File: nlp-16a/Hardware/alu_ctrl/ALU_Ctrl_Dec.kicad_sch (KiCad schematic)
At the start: 9 parts, among them U19 CD74HC00, U20 CD74HC00, U21 CD74HC00, U22 CD74HC00, U23 CD74HC00, U24 CD74HC00, U25 CD74HC00, U26 CD74HC00, U27 CD74HC00

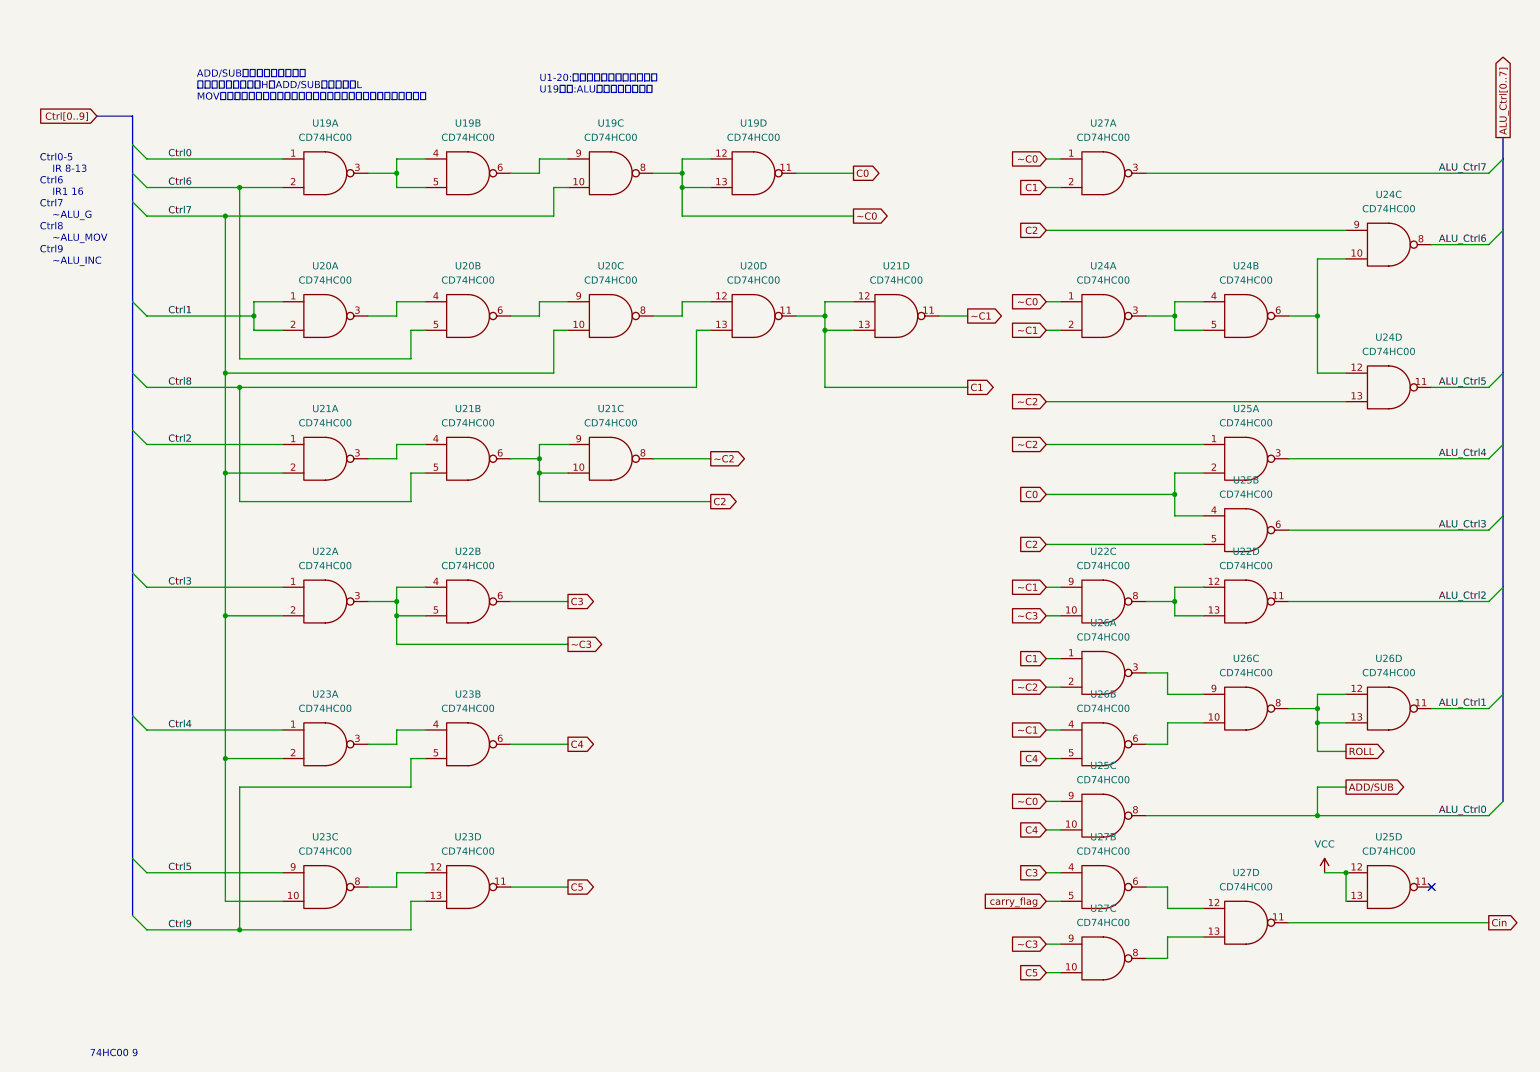
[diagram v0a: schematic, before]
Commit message: ALU制御の回路修正
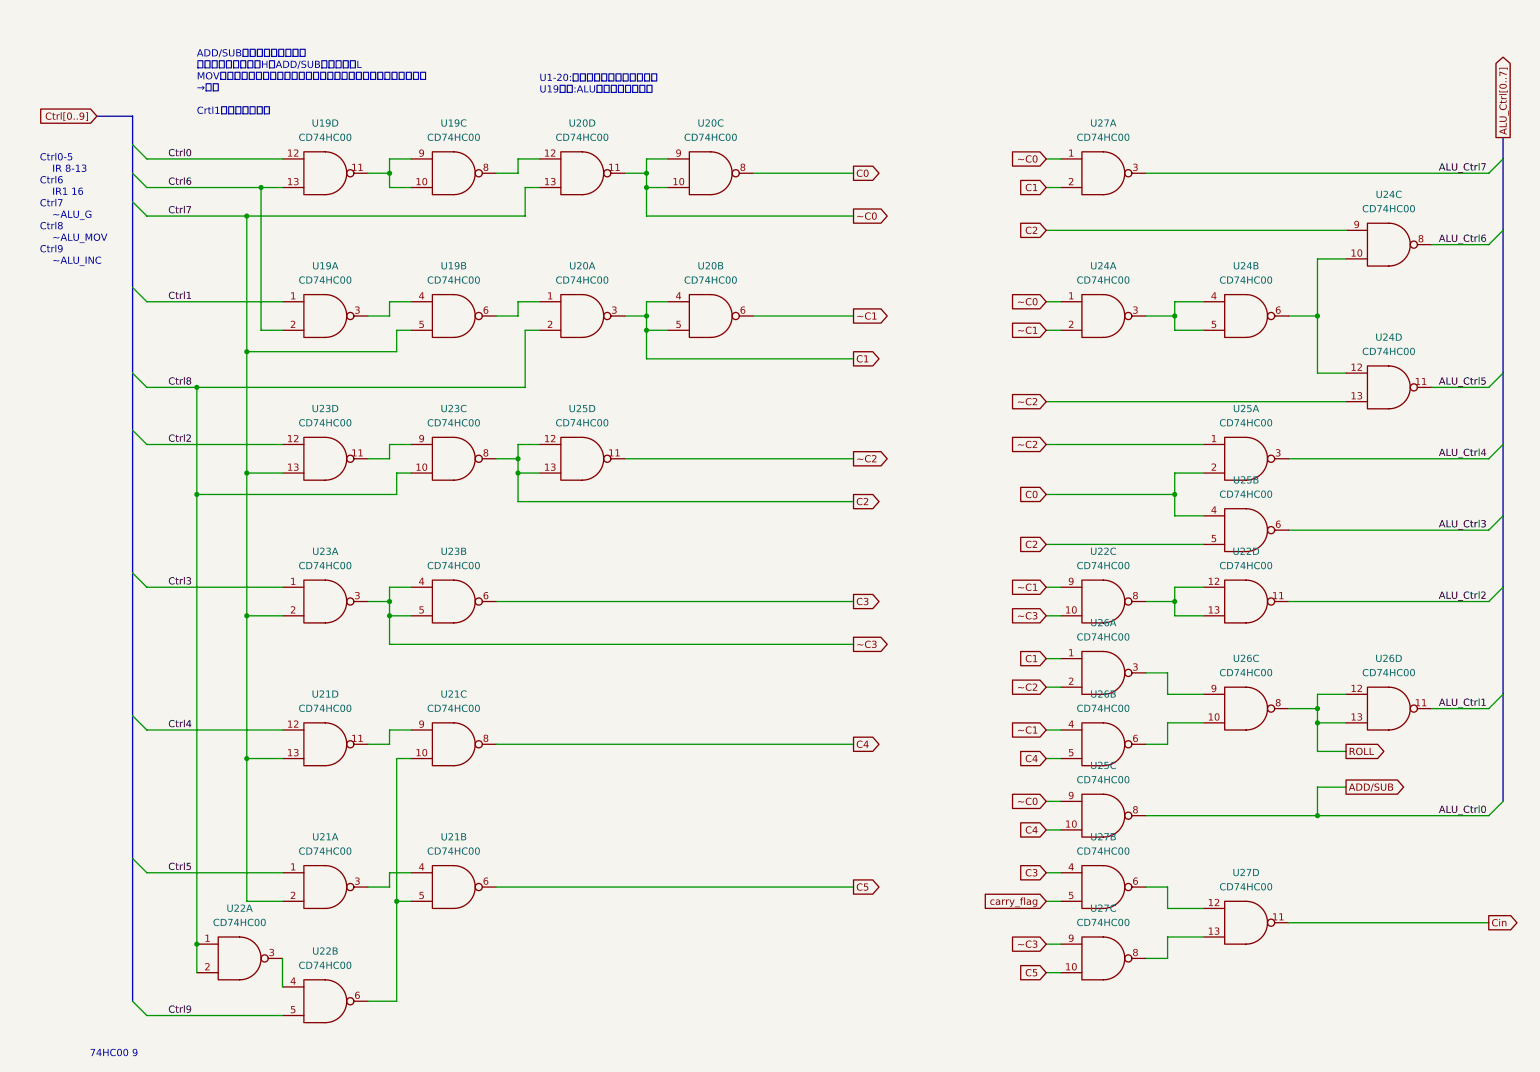
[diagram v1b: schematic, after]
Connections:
- net C0: now also U20.8; no longer U19.11
- net C1: now also U20.3, U20.4, U20.5; no longer U20.11, U21.12, U21.13
- net C2: now also U23.8, U25.12, U25.13; no longer U21.10, U21.6, U21.9
- net C3: now also U23.6; no longer U22.6
- net C4: now also U21.8; no longer U23.6
- net C5: now also U21.6; no longer U23.11
- net Ctrl0: now also U19.12; no longer U19.1
- net Ctrl1: now also U19.1; no longer U20.1, U20.2
- net Ctrl2: now also U23.12; no longer U21.1
- net Ctrl3: now also U23.1; no longer U22.1
- net Ctrl4: now also U21.12; no longer U23.1
- net Ctrl5: now also U21.1; no longer U23.9
- net Ctrl6: now also U19.13; no longer U20.5
- net Ctrl7: now also U19.5, U20.13, U21.13, U23.13; no longer U19.10, U20.10, U22.2, U23.10
- net Ctrl8: now also U20.2, U22.1, U22.2, U23.10; no longer U20.13, U21.5
- net Ctrl9: now also U22.5; no longer U23.13, U23.5
- net VCC: no longer U25.12, U25.13
- net ~C0: now also U20.10, U20.11, U20.9; no longer U19.12, U19.13, U19.8
- net ~C1: now also U20.6; no longer U21.11
- net ~C2: now also U25.11; no longer U21.8
- net ~C3: now also U23.3, U23.4, U23.5; no longer U22.3, U22.4, U22.5
- net at U19.3, U19.4: no longer U19.5
- net at U19.6: now also U20.1; no longer U19.9
- net at U20.12: now also U19.8; no longer U20.8
- new net: U19.10, U19.11, U19.9
- new net: U22.3, U22.4
- new net: U21.10, U21.5, U22.6
- new net: U21.11, U21.9
- new net: U23.11, U23.9
- no-connect marks 1 -> 0
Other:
- note added: "ADD/SUB介入モードに不具合 モード設定が逆通常HでADD/SUBモードのみL MOVモード，通常演算モードに影響を与えない設計にする必要があり →解消 Crtl1デコード不完全"
- note removed: "ADD/SUB介入モードに不具合 モード設定が逆通常HでADD/SUBモードのみL MOVモード，通常演算モードに影響を与えない設計にする必要があり"
- moved on the sheet: U19A, U19B, U19C, U19D, U20A, U20B, U20C, U20D, U21A, U21B, U21C, U21D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

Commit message: ゼロフラグ高速化
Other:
- note added: "ADD/SUB介入モードに不具合 モード設定が逆通常HでADD/SUBモードのみL MOVモード，通常演算モードに影響を与えない設計にする必要があり →解消 Crtl1デコード不完全→解消 最終版→Ctrl1は反転とする．"
- note added: "Ctrl0-5 IR 8-13 Ctrl6 ADDRESS_MODE(IR1 15) Ctrl7 ~INTERNAL_MOV Ctrl8 ~INTERNAL_INC Ctrl9 ~INTERNAL_DEC ADDRESS_MODE: アドレッシング時の演算モードに切り替え．演算命令以外でこのモードになる． INTERNAL_MOV: 内部処理での値を移動するときのモード． ADDRESS_MODEより優先される． INTERNAI_INC: 内部処理でインクリメントするときのモード． このモードを使用する際にはINTERNAL_MOVが有効である必要がある． ADDRESS_MODEより優先される． INTERNAI_INC: 内部処理でデクリメントするときのモード． このモードを使用する際にはINTERNAL_MOV，INTERNAL_INCが有効である必要がある． ADDRESS_M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"
- note removed: "ADD/SUB介入モードに不具合 モード設定が逆通常HでADD/SUBモードのみL MOVモード，通常演算モードに影響を与えない設計にする必要があり →解消 Crtl1デコード不完全"
- note removed: "Ctrl0-5 IR 8-13 Ctrl6 IR1 16 Ctrl7 ~ALU_G Ctrl8 ~ALU_MOV Ctrl9 ~ALU_INC"
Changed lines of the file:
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@@
     (effects (font (size 1.27 1.27)) (justify left bottom))
   )
-  (text "ADD/SUB介入モードに不具合\nモード設定が逆通常HでADD/SUBモードのみL\nMOVモード，通常演算モードに影響を与えない設計にする必要があり\n→解消\n\nCrtl1デコード不完全"
+  (text "ADD/SUB介入モードに不具合\nモード設定が逆通常HでADD/SUBモードのみL\nMOVモード，通常演算モードに影響を与えない設計にする必要があり\n→解消\n\nCrtl1デコード不完全→解消\n\n最終版→Ctrl1は反転とする．"
     (at 41.91 25.4 0)
     (effects (font (size 1.27 1.27)) (justify left bottom))
   )
-  (text "Ctrl0-5\n	IR 8-13\nCtrl6\n	IR1 16\nCtrl7\n	~ALU_G\nCtrl8\n	~ALU_MOV\nCtrl9\n	~ALU_INC"
-    (at 13.97 52.07 0)
+  (text "Ctrl0-5\n	IR 8-13\nCtrl6\n	ADDRESS_MODE(IR1 15)\nCtrl7\n	~INTERNAL_MOV\nCtrl8\n	~INTERNAL_INC\nCtrl9\n	~INTERNAL_DEC\n\nADDRESS_MODE:\n	アドレッシング時の演算モードに切り替え．演算命令以外でこのモードになる．\nINTERNAL_MOV:\n	内部処理での値を移動するときのモード．\n	ADDRESS_MODEより優先される．\nINTERNAI_INC:\n	内部処理でインクリメントするときのモード．\n	このモードを使用する際にはINTERNAL_MOVが有効である必要がある．\n	ADDRESS_MODEより優先される．\nINTERNAI_INC:\n	内部処理でデクリメントするときのモード．\n	このモードを使用する際にはINTERNAL_MOV，INTERNAL_INCが有効である必要がある．\n	ADDRESS_MODEより優先される．"
+    (at 102.87 189.23 0)
     (effects (font (size 1.27 1.27)) (justify left bottom))
   )

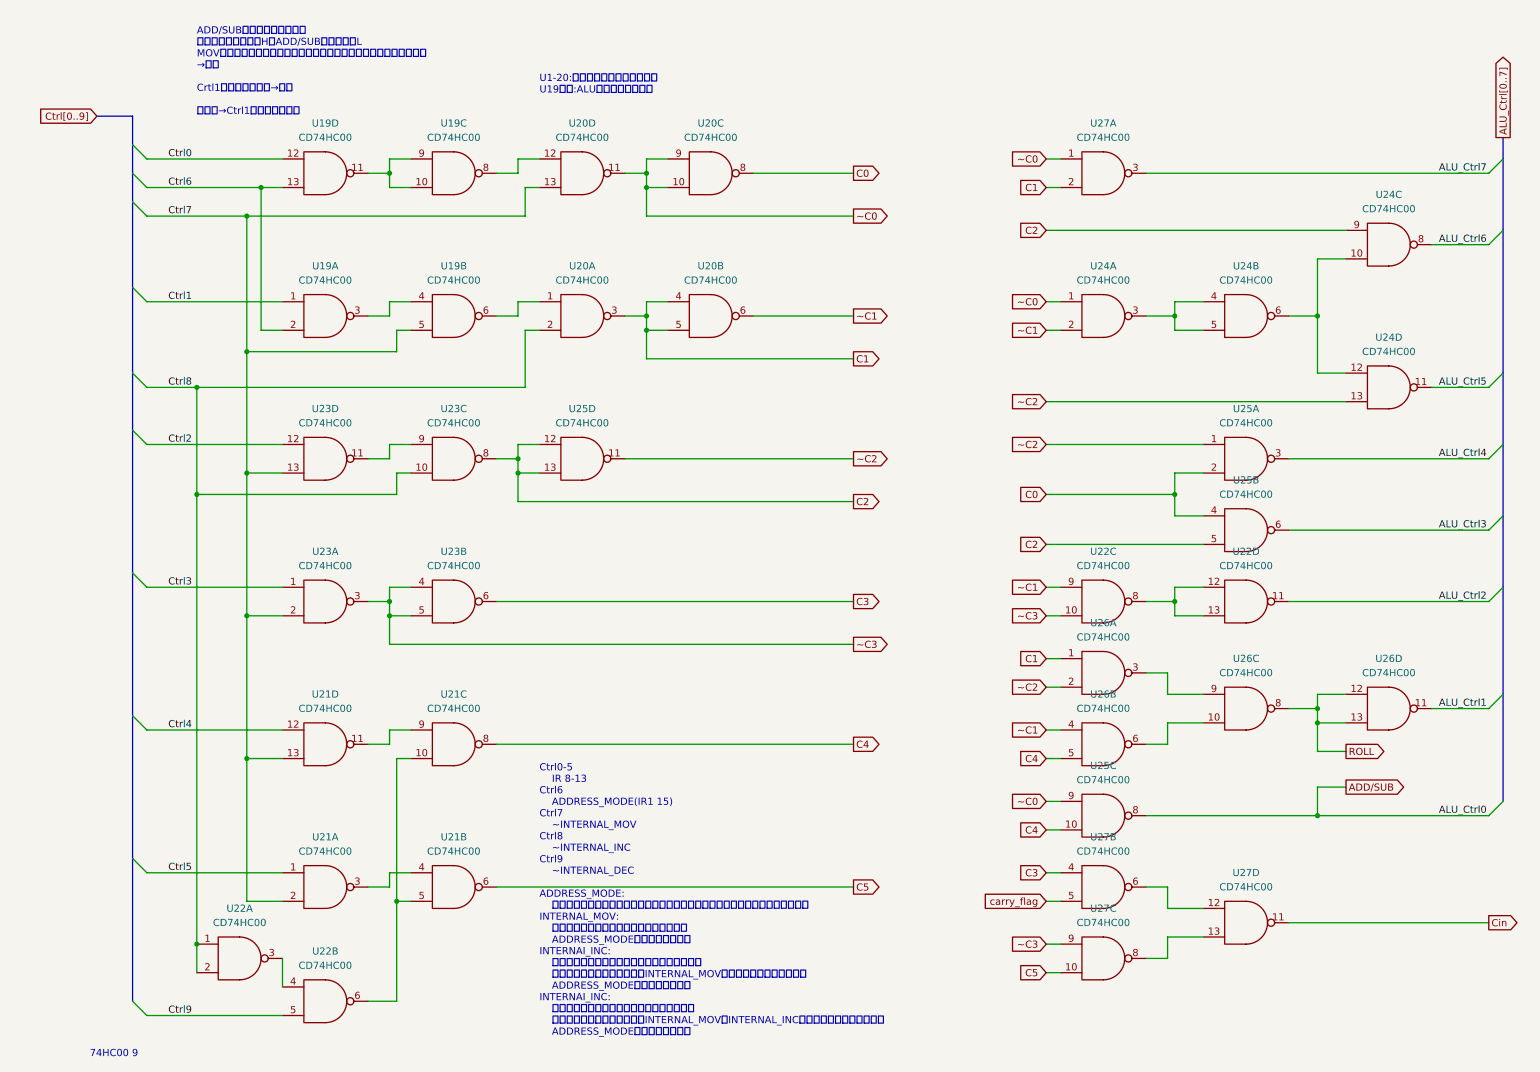
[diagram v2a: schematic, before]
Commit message: 基板の途中経過(デコーダ部分を配線中)
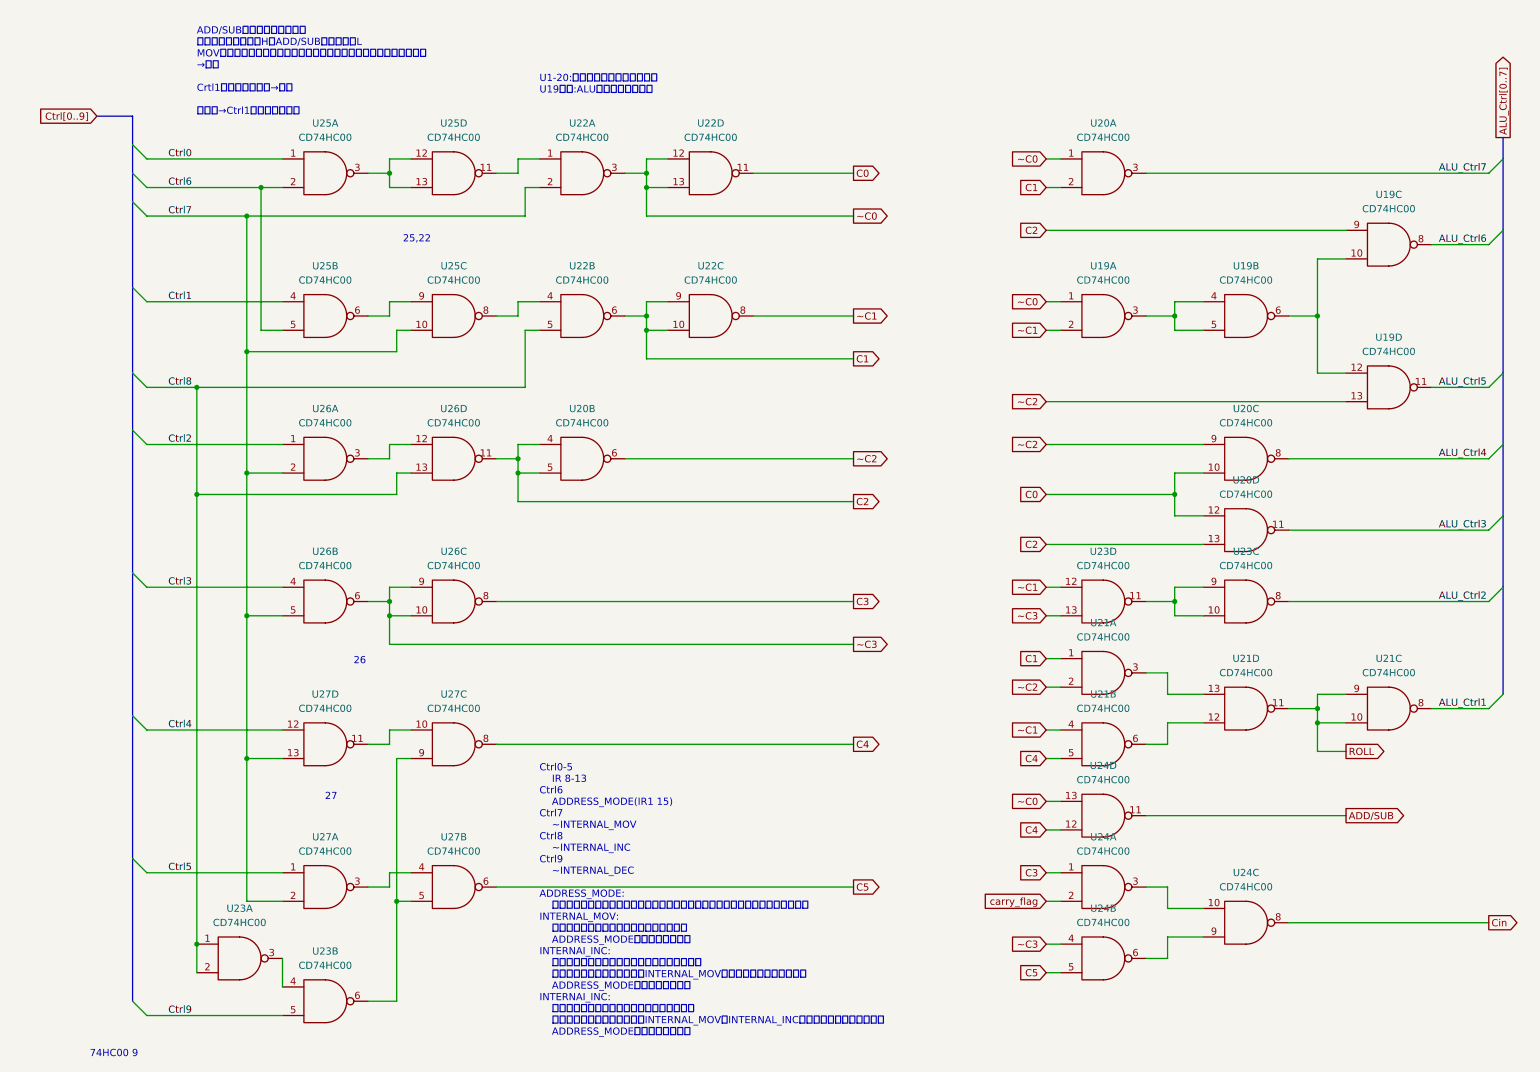
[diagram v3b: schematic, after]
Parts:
- renumbered U24 to U19, U25 to U20, U27 to U20, U26 to U21, U20 to U22, U22 to U23, U25 to U24, U27 to U24, U19 to U25, U23 to U26, U21 to U27
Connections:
- net ADD/SUB: now also U24.11; no longer U24.8
- net ALU_Ctrl1: now also U21.8; no longer U21.11
- net ALU_Ctrl2: now also U23.8; no longer U23.11
- net ALU_Ctrl3: now also U20.11; no longer U20.6
- net ALU_Ctrl4: now also U20.8; no longer U20.3
- net C0: now also U20.10, U20.12, U22.11; no longer U20.2, U20.4, U22.8
- net C1: now also U22.10, U22.6, U22.9; no longer U22.3, U22.4, U22.5
- net C2: now also U20.13, U20.4, U20.5, U26.11; no longer U20.12, U20.13, U20.5, U26.8
- net C3: now also U24.1, U26.8; no longer U24.4, U26.6
- net C4: now also U24.12; no longer U24.10
- net C5: now also U24.5; no longer U24.10
- net Cin: now also U24.8; no longer U24.11
- net Ctrl0: now also U25.1; no longer U25.12
- net Ctrl1: now also U25.4; no longer U25.1
- net Ctrl2: now also U26.1; no longer U26.12
- net Ctrl3: now also U26.4; no longer U26.1
- net Ctrl6: now also U25.2, U25.5; no longer U25.13, U25.2
- net Ctrl7: now also U22.2, U25.10, U26.2, U26.5; no longer U22.13, U25.5, U26.13, U26.2
- net Ctrl8: now also U22.5, U26.13; no longer U22.2, U26.10
- net ROLL: now also U21.10, U21.11, U21.9; no longer U21.12, U21.13, U21.8
- net carry_flag: now also U24.2; no longer U24.5
- net ~C0: now also U22.12, U22.13, U22.3, U24.13; no longer U22.10, U22.11, U22.9, U24.9
- net ~C1: now also U22.8, U23.12; no longer U22.6, U23.9
- net ~C2: now also U20.6, U20.9; no longer U20.1, U20.11
- net ~C3: now also U23.13, U24.4, U26.10, U26.6, U26.9; no longer U23.10, U24.9, U26.3, U26.4, U26.5
- net at U23.6, U27.5: now also U27.9; no longer U27.10
- net at U21.6: now also U21.12; no longer U21.10
- net at U27.11: now also U27.10; no longer U27.9
- net at U21.3: now also U21.13; no longer U21.9
- new net: U22.4, U25.8
- new net: U25.6, U25.9
- new net: U22.1, U25.11
- new net: U25.12, U25.13, U25.3
- new net: U24.6, U24.9
- new net: U23.10, U23.11, U23.9
- new net: U24.10, U24.3
- new net: U26.12, U26.3
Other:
- note added: "25,22"
- note added: "26"
- note added: "27"

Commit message: 基板の途中経過
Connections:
- net Ctrl4: now also U27.13; no longer U27.12
- net Ctrl5: now also U27.2; no longer U27.1
- net Ctrl7: now also U27.1, U27.12; no longer U27.13, U27.2
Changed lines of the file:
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@@
     (pin "13")
   )
-  (symbol (lib_id "CD74HCxx:CD74HC00") (at 64.77 137.16 0) (unit 4)
+  (symbol (lib_id "CD74HCxx:CD74HC00") (at 64.77 137.16 0) (mirror x) (unit 4)
     (in_bom yes) (on_board yes) (fields_autoplaced)
     (property "Reference" "U27" (id 0) (at 64.77 128.27 0))
@@
     (pin "13")
   )
-  (symbol (lib_id "CD74HCxx:CD74HC00") (at 64.77 162.56 0) (unit 1)
+  (symbol (lib_id "CD74HCxx:CD74HC00") (at 64.77 162.56 0) (mirror x) (unit 1)
     (in_bom yes) (on_board yes) (fields_autoplaced)
     (property "Reference" "U27" (id 0) (at 64.77 153.67 0))

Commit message: ALU制御 修正分反映
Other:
- note added: "ADD/SUB介入モードに不具合 モード設定が逆通常HでADD/SUBモードのみL MOVモード，通常演算モードに影響を与えない設計にする必要があり →解消 Crtl1デコード不完全→解消 最終版→Ctrl1は反転とする． →非反転に設計変更．下記の「削除」修正"
- note added: "削除"
- note removed: "ADD/SUB介入モードに不具合 モード設定が逆通常HでADD/SUBモードのみL MOVモード，通常演算モードに影響を与えない設計にする必要があり →解消 Crtl1デコード不完全→解消 最終版→Ctrl1は反転とする．"
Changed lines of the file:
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@@
+    (stroke (width 0) (type default) (color 0 0 0 0))
+  )
+  (polyline (pts (xy 96.52 27.94) (xy 96.52 52.07))
     (stroke (width 0) (type default) (color 0 0 0 0))
   )
@@
     (stroke (width 0) (type default) (color 0 0 0 0))
   )
+  (polyline (pts (xy 54.61 27.94) (xy 54.61 69.85))
+    (stroke (width 0) (type default) (color 0 0 0 0))
+  )
   (wire (pts (xy 95.25 162.56) (xy 158.75 162.56))
     (stroke (width 0) (type default) (color 0 0 0 0))
@@
     (stroke (width 0) (type default) (color 0 0 0 0))
   )
+  (polyline (pts (xy 96.52 52.07) (xy 76.2 52.07))
+    (stroke (width 0) (type default) (color 0 0 0 0))
+  )
   (bus (pts (xy 30.48 40.64) (xy 30.48 35.56))
     (stroke (width 0) (type default) (color 0 0 0 0))
@@
     (stroke (width 0) (type default) (color 0 0 0 0))
   )
+  (polyline (pts (xy 76.2 52.07) (xy 76.2 69.85))
+    (stroke (width 0) (type default) (color 0 0 0 0))
+  )
   (wire (pts (xy 210.82 111.76) (xy 215.9 111.76))
     (stroke (width 0) (type default) (color 0 0 0 0))
@@
     (stroke (width 0) (type default) (color 0 0 0 0))
   )
+  (polyline (pts (xy 54.61 27.94) (xy 96.52 27.94))
+    (stroke (width 0) (type default) (color 0 0 0 0))
+  )
   (wire (pts (xy 76.2 35.56) (xy 76.2 33.02))
     (stroke (width 0) (type default) (color 0 0 0 0))
@@
     (stroke (width 0) (type default) (color 0 0 0 0))
   )
+  (polyline (pts (xy 76.2 69.85) (xy 54.61 69.85))
+    (stroke (width 0) (type default) (color 0 0 0 0))
+  )
   (wire (pts (xy 214.63 166.37) (xy 220.98 166.37))
     (stroke (width 0) (type default) (color 0 0 0 0))
@@
     (effects (font (size 1.27 1.27)) (justify left bottom))
   )
-  (text "ADD/SUB介入モードに不具合\nモード設定が逆通常HでADD/SUBモードのみL\nMOVモード，通常演算モードに影響を与えない設計にする必要があり\n→解消\n\nCrtl1デコード不完全→解消\n\n最終版→Ctrl1は反転とする．"
+  (text "ADD/SUB介入モードに不具合\nモード設定が逆通常HでADD/SUBモードのみL\nMOVモード，通常演算モードに影響を与えない設計にする必要があり\n→解消\n\nCrtl1デコード不完全→解消\n\n最終版→Ctrl1は反転とする．\n      →非反転に設計変更．下記の「削除」修正"
     (at 41.91 25.4 0)
     (effects (font (size 1.27 1.27)) (justify left bottom))
@@
     (effects (font (size 1.27 1.27)) (justify left bottom))
   )
+  (text "削除" (at 72.39 27.94 0)
+    (effects (font (size 1.27 1.27)) (justify left bottom))
+  )
